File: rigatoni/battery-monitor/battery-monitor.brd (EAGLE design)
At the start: 69.8 x 133.3 mm, 26 parts, among them J1 S2B-XH-A_(LF)(SN), J4 S4B-XH-A(LF)(SN), U1 LT1930ES5TRMPBF_BOOST_CONV, U2 NUCLEO-H743ZI-HEADER

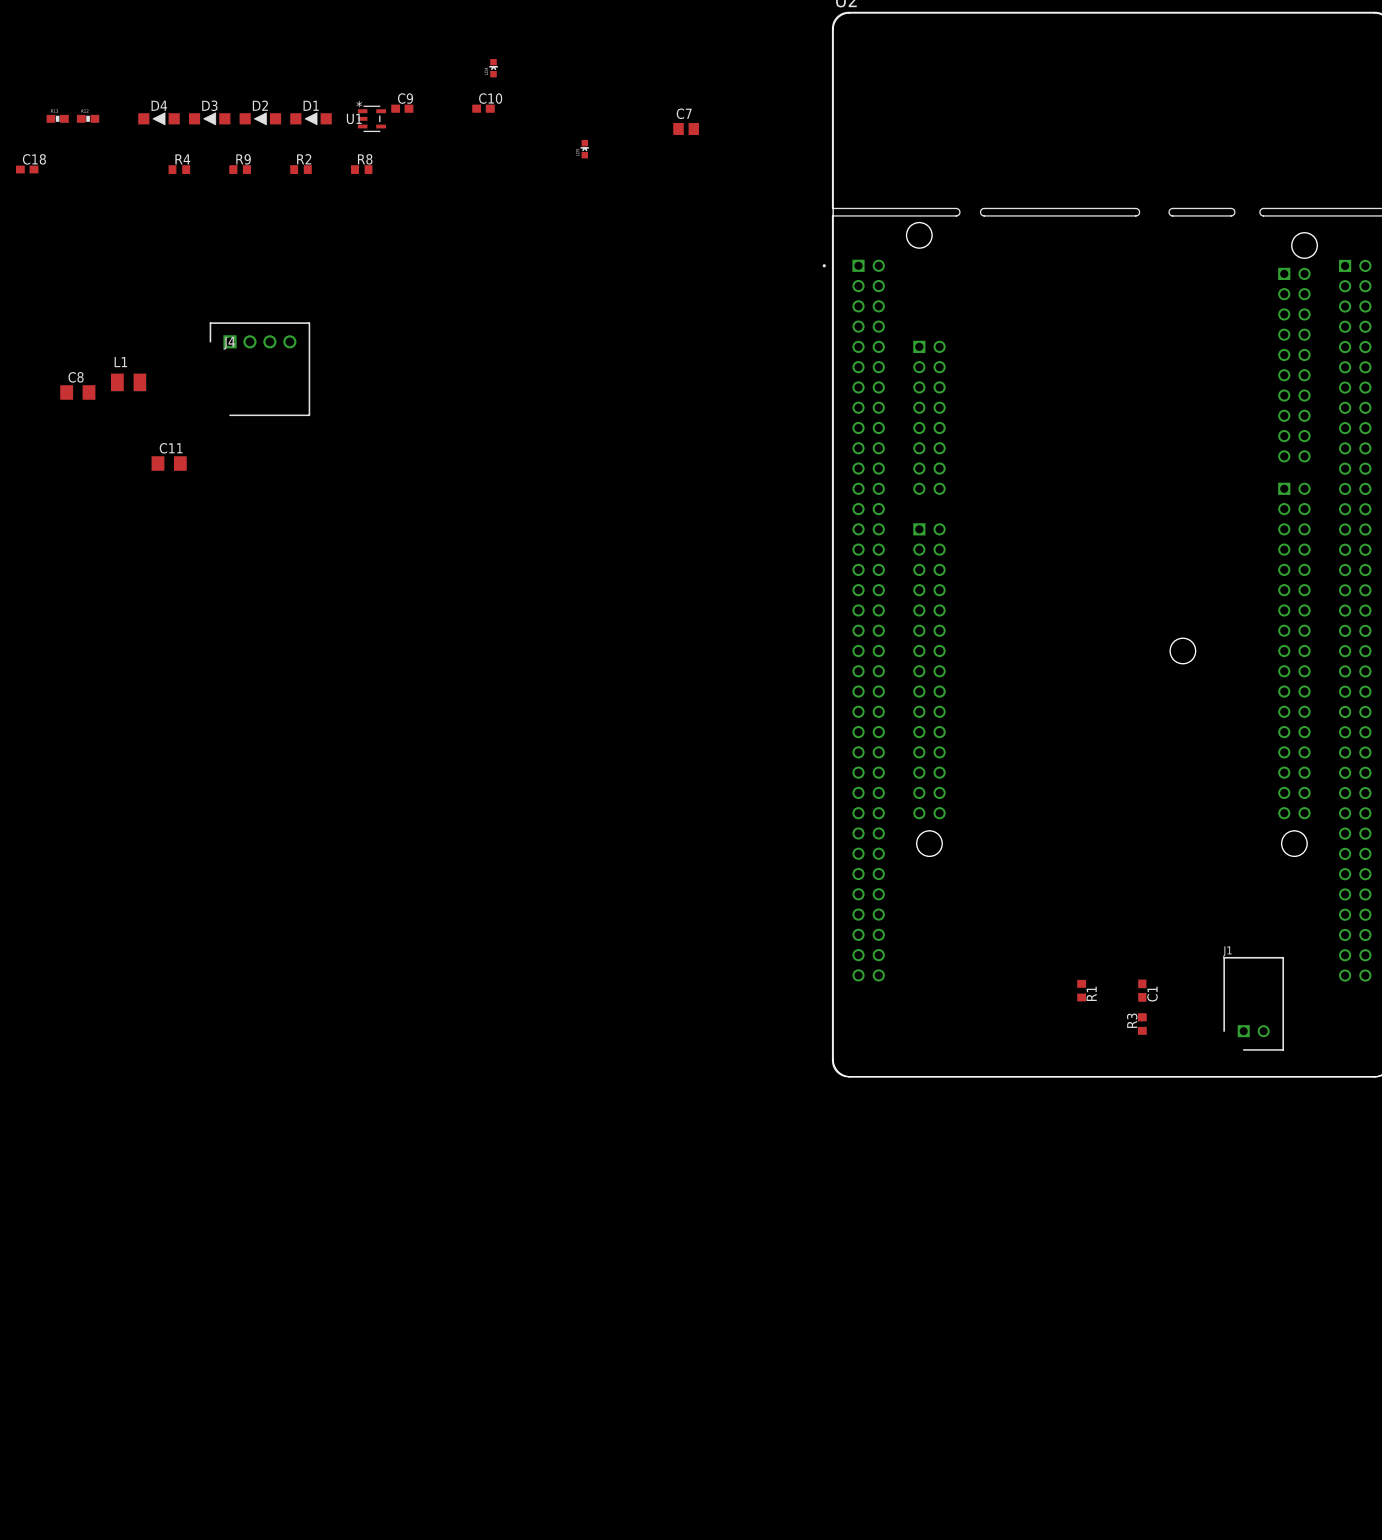
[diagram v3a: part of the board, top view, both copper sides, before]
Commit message: Added 12V to 5V power circuit and LCD connector to schematic
Started to assign pins between the LCD connector and the nucleo header pins
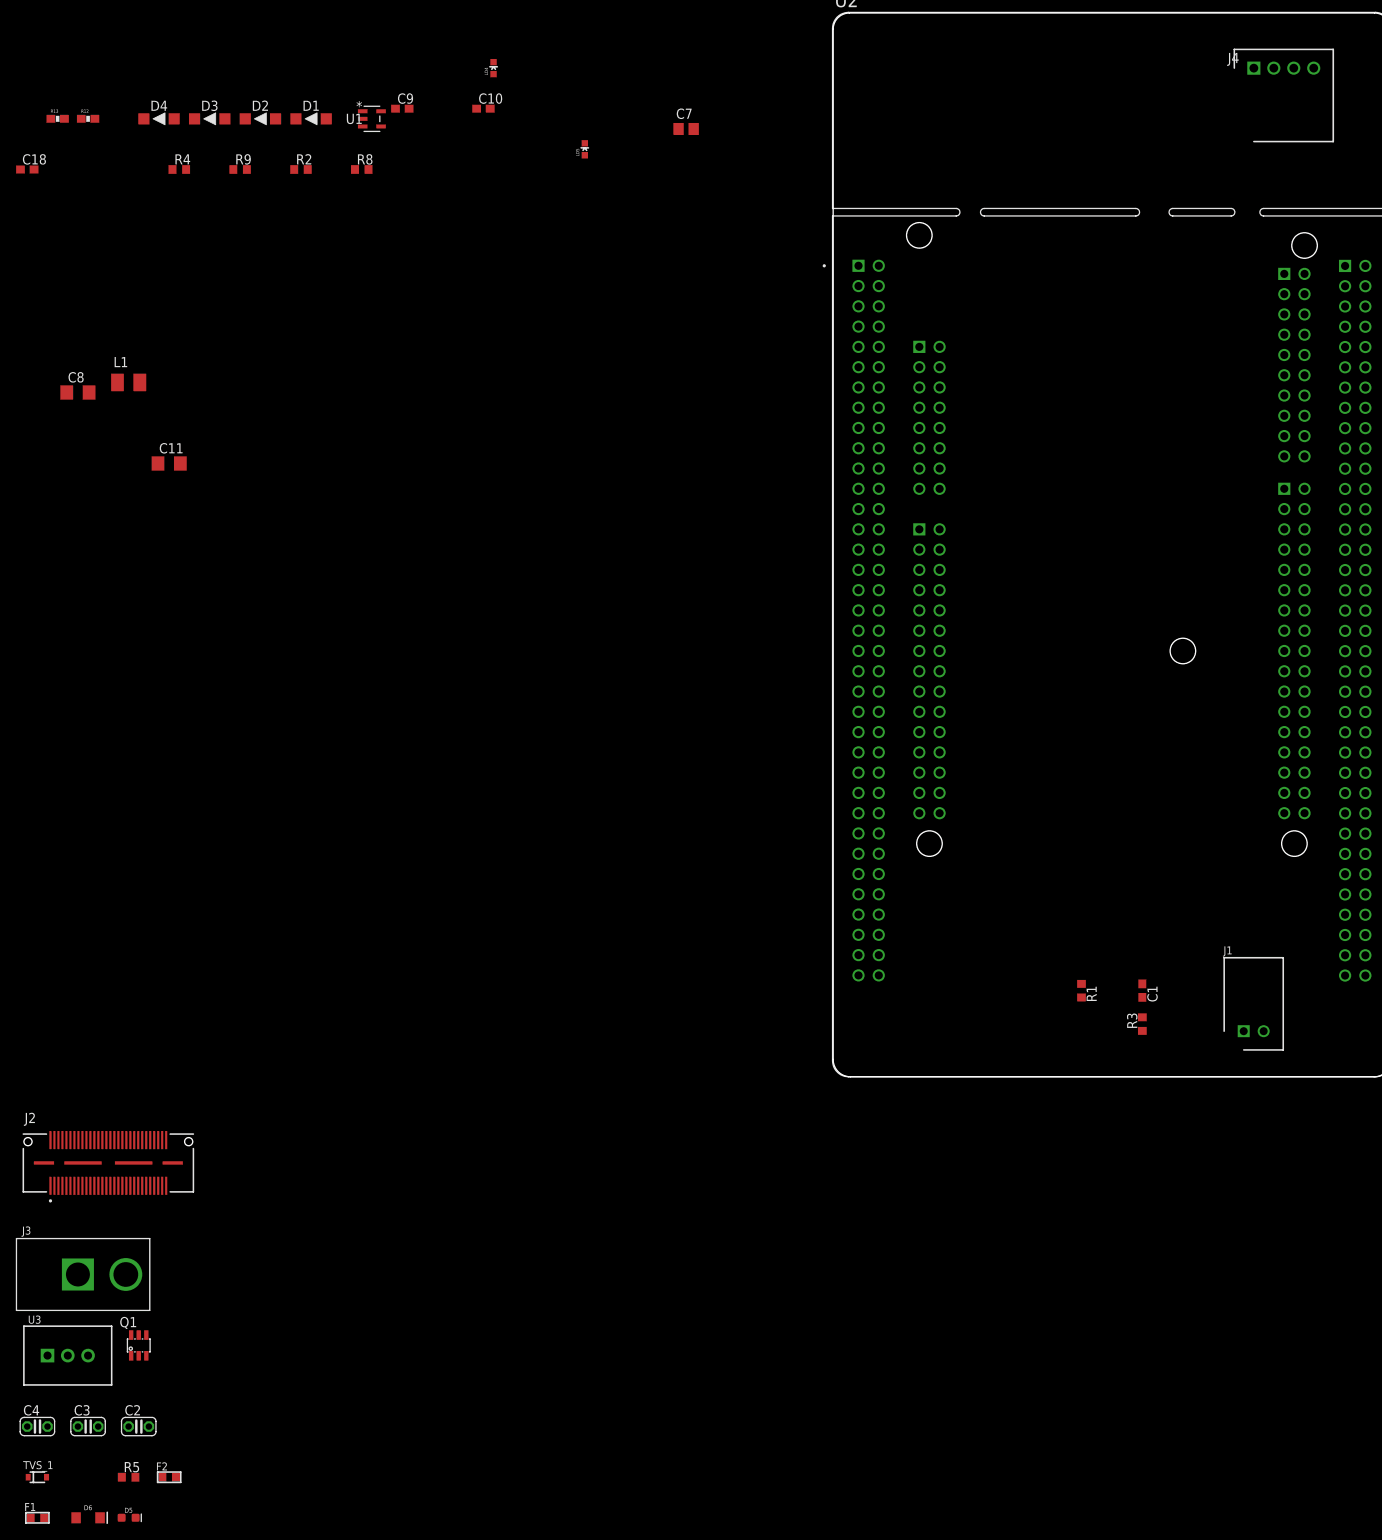
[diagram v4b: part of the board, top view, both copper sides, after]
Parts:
- added C2: 10uF, rcl:C025-024X044
- added C3: 0.1uF, rcl:C025-024X044
- added C4: 100uF, rcl:C025-024X044
- added D5: Yellow, RoboJackets-LEDs:LED-0603
- added D6: GREEN, RoboJackets-LEDs:LED-1206
- added F1: 630mA, RoboJackets-Fuses:F0603
- added F2: 1.875A, RoboJackets-Fuses:F0603
- added J2: QSH-030-01-X-D-A-XX, QSH-030-01-X-D-A-XX:SAMTEC_QSH-030-01-X-D-A-XX
- added J3: (no value), RoboJackets-Connectors:PJ-037A
- added Q1: STT4P3LLH6, RoboJackets-Discrete:SOT23-6
- added R5: 1k, rcl:R0603
- added TVS_1: D5V0L1B2WS-7, RoboJackets-Diodes:SOD-323
- added U3: TPSM84205EAB, RoboRacing_STM:TPSM84205EAB
- moved J4 132.8 mm to (80.0, 99.1)
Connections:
- removed net E5V: U2.CN11_6
- removed net GND_CN11: U2.CN11_19, U2.CN11_20, U2.CN11_22, U2.CN11_49, U2.CN11_60, U2.CN11_71, U2.CN11_72, U2.CN11_8
- new net 5V_MAIN: C4.1, F2.1, U3.VOUT
- new net BLGND: J2.27
- new net BLGND_2: J2.29
- new net BLVDD(+5V): J2.21
- new net BLVDD_2(+5V): J2.23
- new net BL_CTRL: J2.53
- new net DSI_CK_N: J2.05, U2.CN10_6
- new net DSI_CK_P: J2.03, U2.CN10_4
- new net DSI_D0_N: J2.11, U2.CN10_12
- new net DSI_D0_P: J2.09, U2.CN7_20
- new net DSI_D1_N: J2.17, U2.CN10_2
- new net DSI_D1_P: J2.15, U2.CN10_8
- new net DSI_TE: J2.49
- new net I2C_SCL: J2.44
- new net I2C_SDA: J2.40
- new net N$10: D5.C, Q1.1, Q1.2, Q1.5, Q1.6
- new net N$11: D6.A, F2.2
- new net N$2: D5.A, F1.2
- new net N$3: Q1.3, R5.2
- new net N$4: C2.1, Q1.4, TVS_1.C, U3.VIN
- new net N$7: F1.1, J3.P$2
- new net RESET: J2.57
- new net TOUCH_INT: J2.04
- new net VDD(2.8V-3.3V): J2.36
- net +5V: now also C3.1, D6.C, U2.CN11_6
- net GND: now also C2.2, C3.2, C4.2, J2.01, J2.07, J2.13, J2.19, J2.S1, J2.S2, J2.S3, J2.S4, J3.P$1, R5.1, TVS_1.A, U2.CN11_19, U2.CN11_20, U2.CN11_22, U2.CN11_49, U2.CN11_60, U2.CN11_71, U2.CN11_72, U2.CN11_8, U3.GND

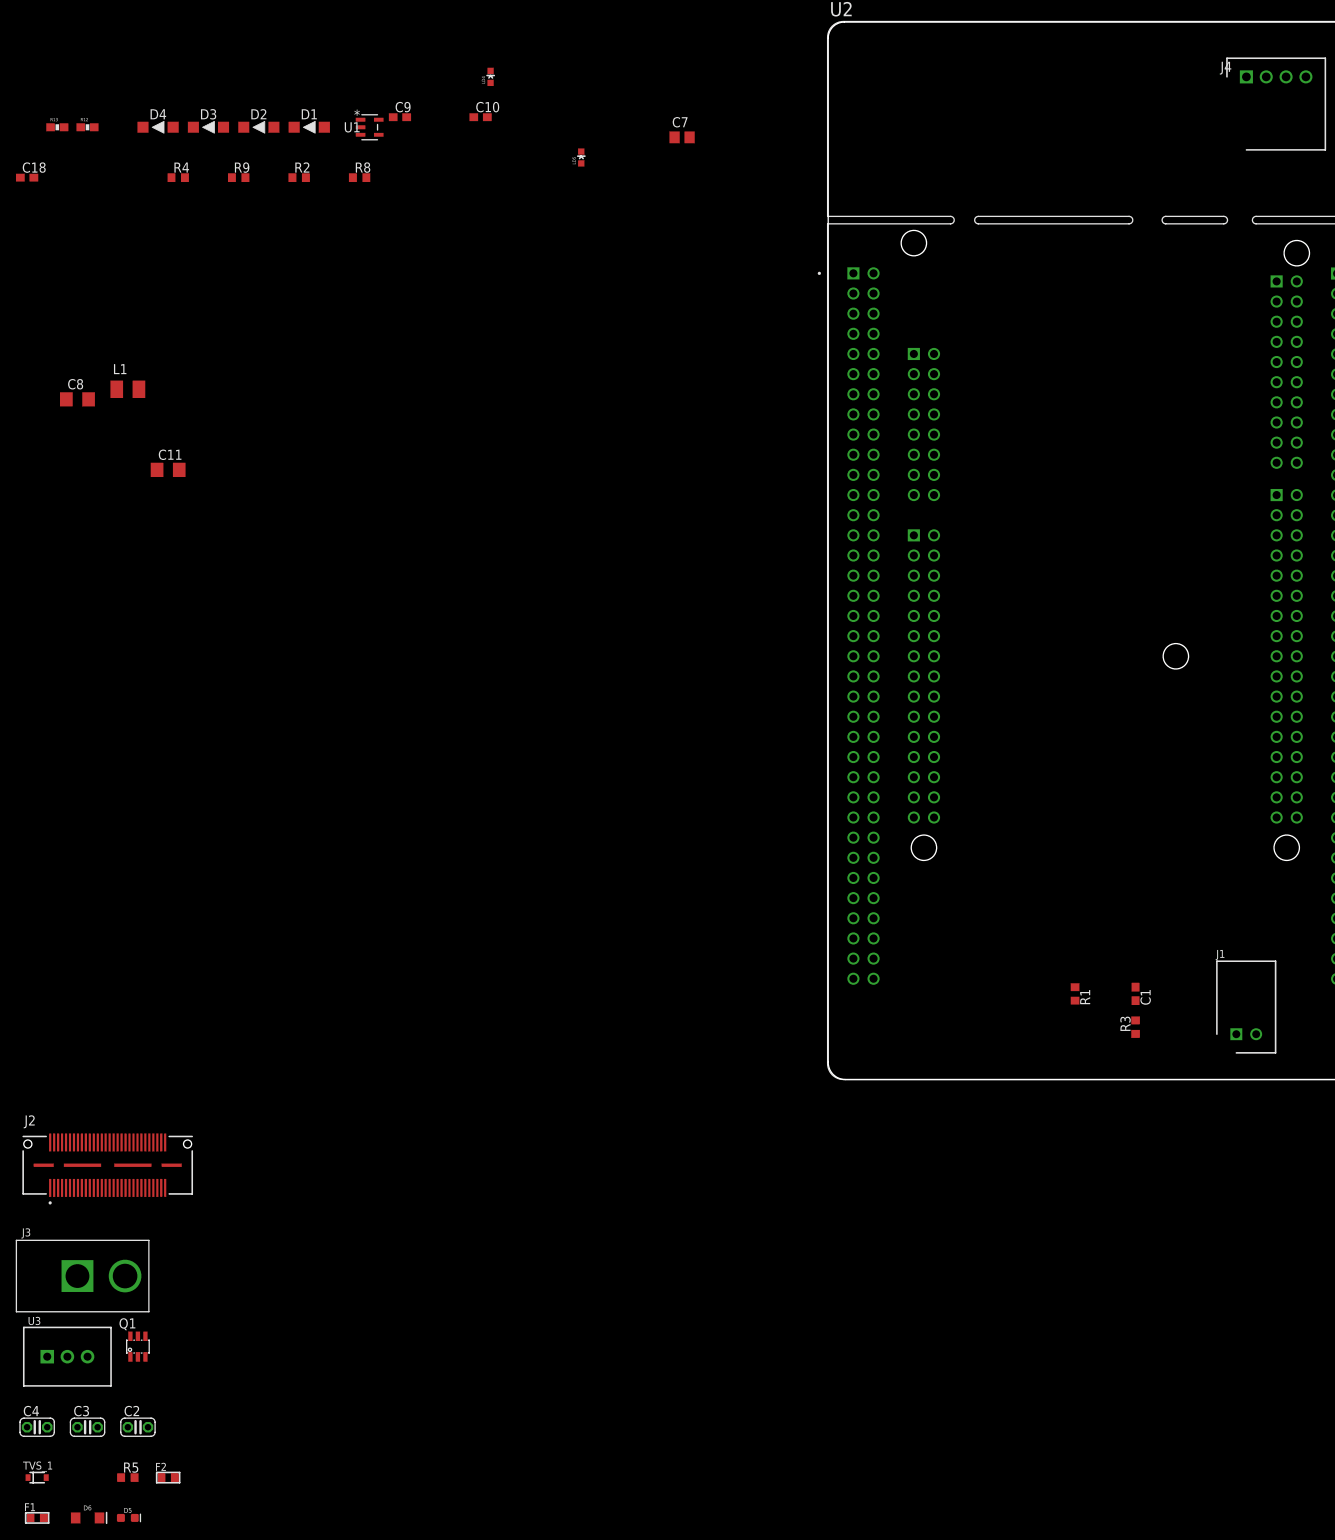
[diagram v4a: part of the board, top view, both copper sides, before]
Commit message: Finished Rough Draft for Schematic Review
Not updated with changes suggested during schematic review
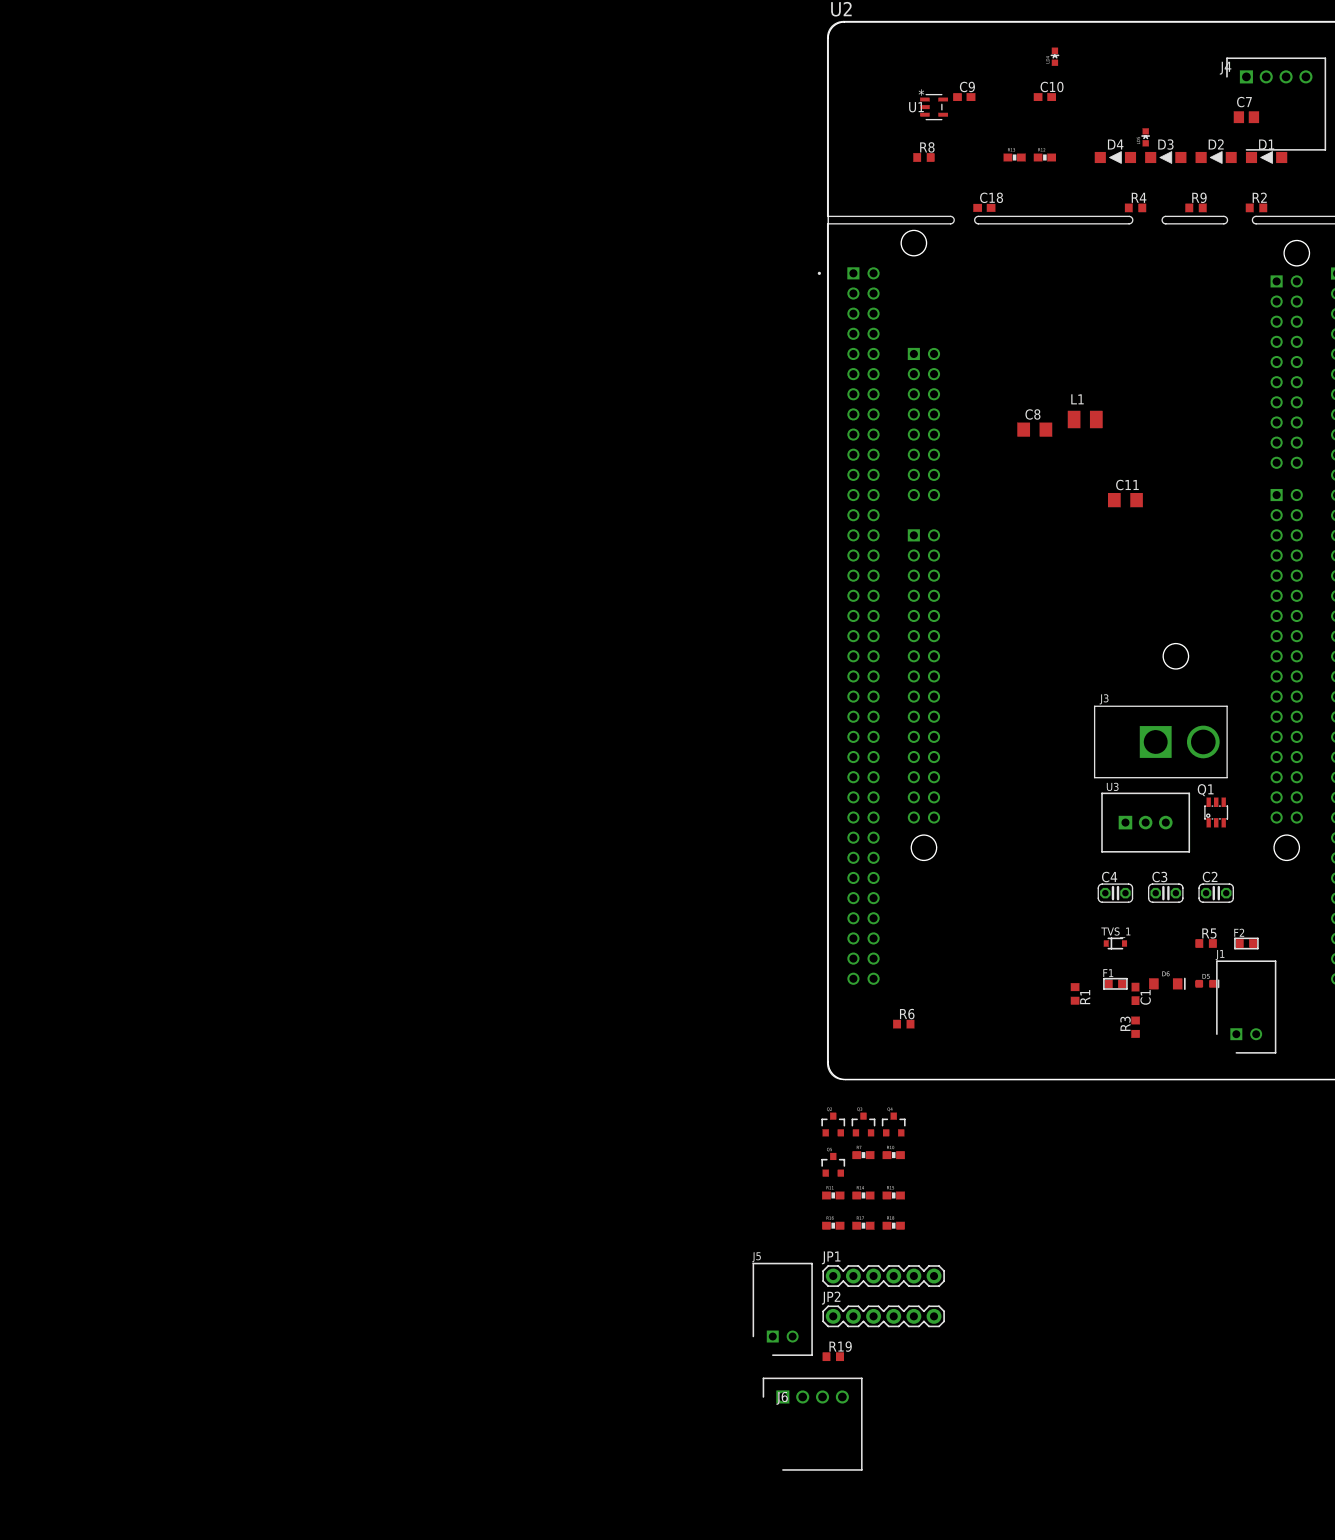
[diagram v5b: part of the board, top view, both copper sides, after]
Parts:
- removed J2: QSH-030-01-X-D-A-XX, QSH-030-01-X-D-A-XX:SAMTEC_QSH-030-01-X-D-A-XX
- added J5: S2B-XH-A_(LF)(SN), drive_brake:SHDR2W80P0X250_1X2_740X1150X61
- added J6: S4B-XH-A(LF)(SN), drive_brake:SHDR4W64P0X250_1X4_1240X1155X7
- added JP1, JP2: (no value), SparkFun:1X06
- added Q2, Q3, Q4, Q5: BSS138, SparkFun:SOT23-3
- added R10, R11, R14, R15, R16, R17, R18, R7: 10K, SparkFun:0603-RES
- added R19: 1k, rcl:R0603
- added R6: 220 Ω, rcl:R0603
- moved C2 151.6 mm to (76.2, -3.81)
- moved C3 151.6 mm to (69.8, -3.81)
- moved C4 151.6 mm to (63.5, -3.81)
- moved D5 151.6 mm to (74.9, -15.2)
- moved D6 151.6 mm to (69.8, -15.2)
- moved F1 151.6 mm to (63.5, -15.2)
- moved F2 151.6 mm to (80.0, -10.2)
- moved J3 151.6 mm to (68.6, 15.2)
- moved Q1 151.6 mm to (76.2, 6.35)
- moved R5 151.6 mm to (74.9, -10.2)
- moved TVS_1 151.6 mm to (63.5, -10.2)
- moved U3 151.6 mm to (67.3, 5.08)
- moved C11 120.7 mm to (64.8, 45.7)
- moved C18 120.7 mm to (47.0, 82.5)
- moved C8 120.7 mm to (53.3, 54.6)
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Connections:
- removed net BLGND: J2.27
- removed net BLGND_2: J2.29
- removed net BLVDD(+5V): J2.21
- removed net BLVDD_2(+5V): J2.23
- removed net BL_CTRL: J2.53
- removed net DSI_CK_N: J2.05, U2.CN10_6
- removed net DSI_CK_P: J2.03, U2.CN10_4
- removed net DSI_D0_N: J2.11, U2.CN10_12
- removed net DSI_D0_P: J2.09, U2.CN7_20
- removed net DSI_D1_N: J2.17, U2.CN10_2
- removed net DSI_D1_P: J2.15, U2.CN10_8
- removed net DSI_TE: J2.49
- removed net N$10: D5.C, Q1.1, Q1.2, Q1.5, Q1.6
- removed net N$11: D6.A, F2.2
- removed net RESET: J2.57
- removed net TOUCH_INT: J2.04
- removed net VDD(2.8V-3.3V): J2.36
- new net HV: JP2.3, R10.1, R14.1, R16.1, R18.1
- new net HV1: JP2.1, Q3.3, R14.2
- new net HV2: JP2.2, Q4.3, R16.2
- new net HV3: JP2.5, Q5.3, R18.2
- new net HV4: JP2.6, Q2.3, R10.2
- new net LED: R6.1, U2.CN9_30
- new net LV: JP1.4, Q2.1, Q3.1, Q4.1, Q5.1, R11.1, R15.1, R17.1, R7.1
- new net LV1: JP1.6, Q3.2, R11.2
- new net LV2: JP1.5, Q4.2, R15.2
- new net LV3: JP1.2, Q5.2, R17.2
- new net LV4: JP1.1, Q2.2, R7.2
- new net N$9: J5.1, R6.2
- net +5V: now also D6.A, F2.2, J6.3
- net GND: now also J5.2, J6.4, JP1.3, JP2.4; no longer J2.01, J2.07, J2.13, J2.19, J2.S1, J2.S2, J2.S3, J2.S4
- net I2C_SCL: now also J6.1, U2.CN7_2; no longer J2.44
- net I2C_SDA: now also J6.2, U2.CN7_4; no longer J2.40
- net N$2: now also D5.C, Q1.1, Q1.2, Q1.5, Q1.6, R19.1
